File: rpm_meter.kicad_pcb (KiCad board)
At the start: 2 copper layers, 191 parts, among them J1 Conn_01x05_Pin, Q1 BC846, Q10 BC857, Q11 BC857, Q12 BC846, Q13 AO3423, Q14 BC846, Q15 BC846, Q16 BC846, Q17 2N7002H, Q18 2N7002H, Q19 2N7002H, Q2 BC857, Q20 2N7002H, Q21 2N7002H, Q22 2N7002H, Q23 2N7002H, Q24 2N7002H, Q25 2N7002H, Q26 2N7002H, Q27 2N7002H, Q28 2N7002H, Q29 2N7002H, Q3 BC857, Q30 2N7002H, Q31 2N7002H, Q32 2N7002H, Q33 2N7002H, Q34 2N7002H, Q35 2N7002H, Q36 2N7002H, Q37 BC857, Q38 BC857, Q39 BC857, Q4 BC857, Q40 BC857, Q41 BC857, Q42 BC857, Q43 BC857, Q44 BC857, Q45 BC857, Q46 BC857, Q5 BC857, Q6 BC857, Q7 BC857, Q8 BC857, Q9 BC857, U1 M24C02-RMN, U2 STM32C031C6Tx, U3 74LVC1G123, Y1 8

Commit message: Shifting registers
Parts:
- removed D23, D26, D29, D32: LED_Dual_AAKK, Library_local:LED_RG_1210
- removed Q11, Q3, Q38, Q40, Q42, Q44, Q46, Q5, Q7, Q9: BC857, Package_TO_SOT_SMD:SOT-23
- removed Q18, Q20, Q22, Q24, Q26, Q28, Q30, Q32, Q34, Q36: 2N7002H, Package_TO_SOT_SMD:SOT-23
- removed R14, R26, R38: 100, Resistor_SMD:R_0603_1608Metric
- removed R15, R27, R39, R81, R82, R87, R88, R93, R94: 10k, Resistor_SMD:R_0603_1608Metric
- removed R20, R32, R44: 91, Resistor_SMD:R_0603_1608Metric
- removed R21, R33, R45, R9: 22, Resistor_SMD:R_0603_1608Metric
- added C17: 100n, Capacitor_SMD:C_0603_1608Metric, F.Cu at (125.4, 46.3)
- added C18: 100n, Capacitor_SMD:C_0603_1608Metric, F.Cu at (125.4, 48.8)
- added C19: 100n, Capacitor_SMD:C_0603_1608Metric, F.Cu at (125.4, 51.3)
- added C20: 100n, Capacitor_SMD:C_0603_1608Metric, F.Cu at (125.4, 53.8)
- added C21: 100n, Capacitor_SMD:C_0603_1608Metric, F.Cu at (125.4, 56.3)
- added D10: LED_Dual_AAKK, Library_local:LED_RG_1210, F.Cu at (166.9, 108.1)
- added D12: LED_Dual_AAKK, Library_local:LED_RG_1210, F.Cu at (118.0, 83.1)
- added D13: LED_Dual_AAKK, Library_local:LED_RG_1210, F.Cu at (177.8, 108.1)
- added D15: LED_Dual_AAKK, Library_local:LED_RG_1210, F.Cu at (143.8, 113.4)
- added D16: LED_Dual_AAKK, Library_local:LED_RG_1210, F.Cu at (156.0, 75.3)
- added D18: LED_Dual_AAKK, Library_local:LED_RG_1210, F.Cu at (166.9, 75.3)
- added D19: LED_Dual_AAKK, Library_local:LED_RG_1210, F.Cu at (188.7, 91.7)
- added D21: LED_Dual_AAKK, Library_local:LED_RG_1210, F.Cu at (188.7, 108.1)
- added D22: LED_Dual_AAKK, Library_local:LED_RG_1210, F.Cu at (187.4, 47.2)
- added D3: LED_Dual_AAKK, Library_local:LED_RG_1210, F.Cu at (177.8, 75.3)
- added D4: LED_Dual_AAKK, Library_local:LED_RG_1210, F.Cu at (156.0, 91.7)
- added D6: LED_Dual_AAKK, Library_local:LED_RG_1210, F.Cu at (143.8, 97.0)
- added D7: LED_Dual_AAKK, Library_local:LED_RG_1210, F.Cu at (188.7, 75.3)
- added D9: LED_Dual_AAKK, Library_local:LED_RG_1210, F.Cu at (156.0, 108.1)
- added IC1: STPIC6D595TTR, Library_local:SOP65P640X120-16N, F.Cu at (118.9, 48.5)
- added IC2: STPIC6D595TTR, Library_local:SOP65P640X120-16N, F.Cu at (118.9, 55.2)
- added IC3: STPIC6D595TTR, Library_local:SOP65P640X120-16N, F.Cu at (118.9, 62.0)
- added IC4: STPIC6D595TTR, Library_local:SOP65P640X120-16N, F.Cu at (118.9, 68.8)
- added IC5: STPIC6D595TTR, Library_local:SOP65P640X120-16N, F.Cu at (118.9, 75.6)
- added Q47: BC857, Package_TO_SOT_SMD:SOT-23, F.Cu at (176.8, 112.7)
- added Q49: BC857, Package_TO_SOT_SMD:SOT-23, F.Cu at (176.8, 117.3)
- added Q51: BC857, Package_TO_SOT_SMD:SOT-23, F.Cu at (176.8, 96.3)
- added Q53: BC857, Package_TO_SOT_SMD:SOT-23, F.Cu at (176.8, 100.9)
- added Q55: BC857, Package_TO_SOT_SMD:SOT-23, F.Cu at (142.7, 118.0)
- added Q57: BC857, Package_TO_SOT_SMD:SOT-23, F.Cu at (142.7, 122.6)
- added Q59: BC857, Package_TO_SOT_SMD:SOT-23, F.Cu at (155.0, 79.9)
- added Q61: BC857, Package_TO_SOT_SMD:SOT-23, F.Cu at (155.0, 84.5)
- added Q63: BC857, Package_TO_SOT_SMD:SOT-23, F.Cu at (131.8, 101.6)
- added Q65: BC857, Package_TO_SOT_SMD:SOT-23, F.Cu at (131.8, 106.2)
- added Q67: BC857, Package_TO_SOT_SMD:SOT-23, F.Cu at (165.9, 79.9)
- added Q69: BC857, Package_TO_SOT_SMD:SOT-23, F.Cu at (165.9, 84.5)
- added Q71: BC857, Package_TO_SOT_SMD:SOT-23, F.Cu at (187.7, 96.3)
- added Q73: BC857, Package_TO_SOT_SMD:SOT-23, F.Cu at (187.7, 100.9)
- added Q75: BC857, Package_TO_SOT_SMD:SOT-23, F.Cu at (116.9, 104.0)
- added Q77: BC857, Package_TO_SOT_SMD:SOT-23, F.Cu at (116.9, 108.7)
- added Q79: BC857, Package_TO_SOT_SMD:SOT-23, F.Cu at (187.7, 112.7)
- added Q81: BC857, Package_TO_SOT_SMD:SOT-23, F.Cu at (187.7, 117.3)
- added Q83: BC857, Package_TO_SOT_SMD:SOT-23, F.Cu at (186.3, 51.8)
- added Q85: BC857, Package_TO_SOT_SMD:SOT-23, F.Cu at (186.3, 56.4)
- added R101: 91, Resistor_SMD:R_0603_1608Metric, F.Cu at (181.2, 114.1)
- added R102: 22, Resistor_SMD:R_0603_1608Metric, F.Cu at (181.2, 116.6)
- added R103: 100, Resistor_SMD:R_0603_1608Metric, F.Cu at (181.2, 119.1)
- added R104: 10k, Resistor_SMD:R_0603_1608Metric, F.Cu at (181.2, 95.2)
- added R107: 91, Resistor_SMD:R_0603_1608Metric, F.Cu at (181.2, 97.7)
- added R108: 22, Resistor_SMD:R_0603_1608Metric, F.Cu at (181.2, 100.2)
- added R109: 100, Resistor_SMD:R_0603_1608Metric, F.Cu at (181.2, 102.7)
- added R110: 10k, Resistor_SMD:R_0603_1608Metric, F.Cu at (147.2, 116.8)
- added R113: 91, Resistor_SMD:R_0603_1608Metric, F.Cu at (147.2, 119.3)
- added R114: 22, Resistor_SMD:R_0603_1608Metric, F.Cu at (147.2, 121.8)
- added R115: 100, Resistor_SMD:R_0603_1608Metric, F.Cu at (147.2, 124.4)
- added R116: 10k, Resistor_SMD:R_0603_1608Metric, F.Cu at (159.4, 78.8)
- added R119: 91, Resistor_SMD:R_0603_1608Metric, F.Cu at (159.4, 81.3)
- added R120: 22, Resistor_SMD:R_0603_1608Metric, F.Cu at (159.4, 83.8)
- added R121: 100, Resistor_SMD:R_0603_1608Metric, F.Cu at (159.4, 86.3)
- added R122: 10k, Resistor_SMD:R_0603_1608Metric, F.Cu at (136.3, 100.4)
- added R125: 91, Resistor_SMD:R_0603_1608Metric, F.Cu at (136.3, 103.0)
- added R126: 22, Resistor_SMD:R_0603_1608Metric, F.Cu at (136.3, 105.5)
- added R127: 100, Resistor_SMD:R_0603_1608Metric, F.Cu at (136.3, 108.0)
- added R128: 10k, Resistor_SMD:R_0603_1608Metric, F.Cu at (170.3, 78.8)
- added R131: 91, Resistor_SMD:R_0603_1608Metric, F.Cu at (170.3, 81.3)
- added R132: 22, Resistor_SMD:R_0603_1608Metric, F.Cu at (170.3, 83.8)
- added R133: 100, Resistor_SMD:R_0603_1608Metric, F.Cu at (170.3, 86.3)
- added R134: 10k, Resistor_SMD:R_0603_1608Metric, F.Cu at (192.1, 95.2)
- added R137: 91, Resistor_SMD:R_0603_1608Metric, F.Cu at (192.1, 97.7)
- added R138: 22, Resistor_SMD:R_0603_1608Metric, F.Cu at (192.1, 100.2)
- added R139: 100, Resistor_SMD:R_0603_1608Metric, F.Cu at (192.1, 102.7)
- added R140: 10k, Resistor_SMD:R_0603_1608Metric, F.Cu at (121.4, 102.9)
- added R143: 91, Resistor_SMD:R_0603_1608Metric, F.Cu at (121.4, 105.4)
- added R144: 22, Resistor_SMD:R_0603_1608Metric, F.Cu at (121.4, 107.9)
- added R145: 100, Resistor_SMD:R_0603_1608Metric, F.Cu at (121.4, 110.4)
- added R146: 10k, Resistor_SMD:R_0603_1608Metric, F.Cu at (192.1, 111.6)
- added R149: 91, Resistor_SMD:R_0603_1608Metric, F.Cu at (192.1, 114.1)
- added R150: 22, Resistor_SMD:R_0603_1608Metric, F.Cu at (192.1, 116.6)
- added R151: 100, Resistor_SMD:R_0603_1608Metric, F.Cu at (192.1, 119.1)
- added R152: 10k, Resistor_SMD:R_0603_1608Metric, F.Cu at (190.8, 50.6)
- added R155: 91, Resistor_SMD:R_0603_1608Metric, F.Cu at (190.8, 53.1)
- added R156: 22, Resistor_SMD:R_0603_1608Metric, F.Cu at (190.8, 55.6)
- added R157: 100, Resistor_SMD:R_0603_1608Metric, F.Cu at (190.8, 58.2)
- added R98: 10k, Resistor_SMD:R_0603_1608Metric, F.Cu at (181.2, 111.6)
- Q17, Q19, Q21, Q23, Q25, Q27, Q29, Q31, Q33, Q35: value 2N7002H -> BC857
- R10, R22, R34, R46: value 100 -> 91
- R11, R23, R35, R78, R84, R90, R96: value 10k -> 22
- R12, R24, R36: value 91 -> 100
- R13, R25, R37: value 22 -> 10k
- R79, R85, R91, R97: value 10k -> 100
- R8: value 91 -> 10k
- R83, R89, R95: value 10k -> 91
- moved R8 89.5 mm to (125.4, 58.8)
- moved C2 86.6 mm to (175.0, 48.8)
- moved D2 86.6 mm to (179.3, 58.9)
- moved R3 86.6 mm to (175.0, 56.3)
- moved R6 86.6 mm to (175.0, 63.9)
- moved TP1 86.6 mm to (179.3, 47.4)
- moved C1 86.6 mm to (175.0, 46.3)
- moved D1 86.6 mm to (179.3, 55.8)
- moved Q1 86.6 mm to (179.5, 62.8)
- moved R1 86.6 mm to (175.0, 51.3)
- moved R2 86.6 mm to (175.0, 53.8)
- moved R4 86.6 mm to (175.0, 58.8)
- moved TP2 86.6 mm to (179.3, 52.0)
- moved R5 86.6 mm to (175.0, 61.3)
- moved D5 70.4 mm to (118.0, 115.8)
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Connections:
- net /led_segment3/led_net_2_1 renamed /Leds/led_segment11/led_net_2_1
- net /led_segment5/led_net_2_1 renamed /Leds/led_segment17/led_net_2_1
- D11 pad 1: /led_segment2/led_net_2_1 -> /Leds/led_segment8/led_net_2_1
- D11 pad 2: /led_segment2/led_net_2_1 -> /Leds/led_segment8/led_net_2_1
- D11 pad 3: /led_segment2/led_net_2_2 -> /Leds/led_segment8/led_net_2_2
- D11 pad 4: /led_segment2/led_net_2_4 -> /Leds/led_segment8/led_net_2_4
- D14 pad 3: /led_segment3/led_net_2_2 -> /Leds/led_segment11/led_net_2_2
- D14 pad 4: /led_segment3/led_net_2_4 -> /Leds/led_segment11/led_net_2_4
- D17 pad 1: /led_segment4/led_net_2_1 -> /Leds/led_segment14/led_net_2_1
- D17 pad 2: /led_segment4/led_net_2_1 -> /Leds/led_segment14/led_net_2_1
- D17 pad 3: /led_segment4/led_net_2_2 -> /Leds/led_segment14/led_net_2_2
- D17 pad 4: /led_segment4/led_net_2_4 -> /Leds/led_segment14/led_net_2_4
- D20 pad 3: /led_segment5/led_net_2_2 -> /Leds/led_segment17/led_net_2_2
- D20 pad 4: /led_segment5/led_net_2_4 -> /Leds/led_segment17/led_net_2_4
- D5 pad 1: /led_segment0/led_net_2_1 -> /Leds/led_segment2/led_net_2_1
- D5 pad 2: /led_segment0/led_net_2_1 -> /Leds/led_segment2/led_net_2_1
- D5 pad 3: /led_segment0/led_net_2_2 -> /Leds/led_segment2/led_net_2_2
- D5 pad 4: /led_segment0/led_net_2_4 -> /Leds/led_segment2/led_net_2_4
- D8 pad 1: /led_segment1/led_net_2_1 -> /Leds/led_segment5/led_net_2_1
- D8 pad 2: /led_segment1/led_net_2_1 -> /Leds/led_segment5/led_net_2_1
- D8 pad 3: /led_segment1/led_net_2_2 -> /Leds/led_segment5/led_net_2_2
- D8 pad 4: /led_segment1/led_net_2_4 -> /Leds/led_segment5/led_net_2_4
- Q10 pad 1: Net-(Q10-B) -> /Leds/led_segment2/led_net_1_1
- Q10 pad 2: /led_segment8/led_net_1_1 -> +5V_led
- Q10 pad 3: /led_segment8/led_net_2_1 -> Net-(Q10-C)
- Q17 pad 1: Net-(Q17-G) -> Net-(Q10-C)
- Q17 pad 2: GND -> /Leds/led_segment2/led_net_1_1
- Q17 pad 3: /led_segment0/led_net_2_5 -> /Leds/led_segment2/led_net_2_1
- Q19 pad 1: Net-(Q19-G) -> /Leds/led_segment3/led_net_1_1
- Q19 pad 2: GND -> +5V_led
- Q19 pad 3: /led_segment2/led_net_2_5 -> Net-(Q19-C)
- Q2 pad 1: Net-(Q2-B) -> /Leds/led_segment0/led_net_1_1
- Q2 pad 2: /led_segment0/led_net_1_1 -> +5V_led
- Q2 pad 3: /led_segment0/led_net_2_1 -> Net-(Q2-C)
- Q21 pad 1: Net-(Q21-G) -> Net-(Q19-C)
- Q21 pad 2: GND -> /Leds/led_segment3/led_net_1_1
- Q21 pad 3: /led_segment4/led_net_2_5 -> /Leds/led_segment3/led_net_2_1
- Q23 pad 1: Net-(Q23-G) -> /Leds/led_segment4/led_net_1_1
- Q23 pad 2: GND -> +5V_led
- Q23 pad 3: /led_segment6/led_net_2_5 -> Net-(Q23-C)
- Q25 pad 1: Net-(Q25-G) -> Net-(Q23-C)
- Q25 pad 2: GND -> /Leds/led_segment4/led_net_1_1
- Q25 pad 3: /led_segment8/led_net_2_5 -> /Leds/led_segment4/led_net_2_1
- Q27 pad 1: Net-(Q27-G) -> /Leds/led_segment5/led_net_1_1
- Q27 pad 2: GND -> +5V_led
- Q27 pad 3: /led_segment0/led_net_2_3 -> Net-(Q27-C)
- Q29 pad 1: Net-(Q29-G) -> Net-(Q27-C)
- Q29 pad 2: GND -> /Leds/led_segment5/led_net_1_1
- Q29 pad 3: /led_segment2/led_net_2_3 -> /Leds/led_segment5/led_net_2_1
- Q31 pad 1: Net-(Q31-G) -> /Leds/led_segment6/led_net_1_1
- Q31 pad 2: GND -> +5V_led
- Q31 pad 3: /led_segment4/led_net_2_3 -> Net-(Q31-C)
- Q33 pad 1: Net-(Q33-G) -> Net-(Q31-C)
- Q33 pad 2: GND -> /Leds/led_segment6/led_net_1_1
- Q33 pad 3: /led_segment6/led_net_2_3 -> /Leds/led_segment6/led_net_2_1
- Q35 pad 1: Net-(Q35-G) -> /Leds/led_segment7/led_net_1_1
- Q35 pad 2: GND -> +5V_led
- Q35 pad 3: /led_segment8/led_net_2_3 -> Net-(Q35-C)
- Q37 pad 1: /led_segment0/led_net_1_1 -> Net-(Q35-C)
- Q37 pad 2: +5V_led -> /Leds/led_segment7/led_net_1_1
- Q37 pad 3: Net-(Q2-B) -> /Leds/led_segment7/led_net_2_1
- Q39 pad 1: /led_segment2/led_net_1_1 -> /Leds/led_segment8/led_net_1_1
- Q4 pad 1: Net-(Q39-C) -> Net-(Q2-C)
- Q4 pad 2: /led_segment2/led_net_1_1 -> /Leds/led_segment0/led_net_1_1
- Q4 pad 3: /led_segment2/led_net_2_1 -> /Leds/led_segment0/led_net_2_1
- Q41 pad 1: /led_segment4/led_net_1_1 -> Net-(Q39-C)
- Q41 pad 2: +5V_led -> /Leds/led_segment8/led_net_1_1
- Q41 pad 3: Net-(Q41-C) -> /Leds/led_segment8/led_net_2_1
- Q43 pad 1: /led_segment6/led_net_1_1 -> /Leds/led_segment9/led_net_1_1
- Q45 pad 1: /led_segment8/led_net_1_1 -> Net-(Q43-C)
- Q45 pad 2: +5V_led -> /Leds/led_segment9/led_net_1_1
- Q45 pad 3: Net-(Q10-B) -> /Leds/led_segment9/led_net_2_1
- Q6 pad 1: Net-(Q41-C) -> /Leds/led_segment1/led_net_1_1
- Q6 pad 2: /led_segment4/led_net_1_1 -> +5V_led
- Q6 pad 3: /led_segment4/led_net_2_1 -> Net-(Q6-C)
- Q8 pad 1: Net-(Q43-C) -> Net-(Q6-C)
- Q8 pad 2: /led_segment6/led_net_1_1 -> /Leds/led_segment1/led_net_1_1
- Q8 pad 3: /led_segment6/led_net_2_1 -> /Leds/led_segment1/led_net_2_1
- R10 pad 1: /led_segment0/led_net_2_2 -> /Leds/led_segment0/led_net_2_4
- R10 pad 2: /led_segment0/led_net_2_3 -> /Leds/red0
- R11 pad 1: Net-(Q3-B) -> +5V_led
- R11 pad 2: GND -> /Leds/led_segment0/led_net_1_1
- R12 pad 1: /led_segment1/led_net_2_4 -> /Leds/led_segment0/led_net_2_2
- R12 pad 2: /led_segment1/led_net_2_5 -> /Leds/green0
- R13 pad 1: +5V_led -> Net-(Q6-C)
- R13 pad 2: /led_segment1/led_net_1_1 -> GND
- R16 pad 1: /led_segment2/led_net_2_4 -> /Leds/led_segment1/led_net_2_4
- R16 pad 2: /led_segment2/led_net_2_5 -> /Leds/red1
- R17 pad 2: /led_segment2/led_net_1_1 -> /Leds/led_segment1/led_net_1_1
- R18 pad 1: /led_segment2/led_net_2_2 -> /Leds/led_segment1/led_net_2_2
- R18 pad 2: /led_segment2/led_net_2_3 -> /Leds/green1
- R19 pad 1: Net-(Q40-C) -> Net-(Q10-C)
- R22 pad 1: /led_segment3/led_net_2_2 -> /Leds/led_segment2/led_net_2_4
- R22 pad 2: /led_segment3/led_net_2_3 -> /Leds/red2
- R23 pad 1: Net-(Q41-C) -> +5V_led
- R23 pad 2: GND -> /Leds/led_segment2/led_net_1_1
- R24 pad 1: /led_segment4/led_net_2_4 -> /Leds/led_segment2/led_net_2_2
- R24 pad 2: /led_segment4/led_net_2_5 -> /Leds/green2
- R25 pad 1: +5V_led -> Net-(Q19-C)
- R25 pad 2: /led_segment4/led_net_1_1 -> GND
- R28 pad 1: /led_segment5/led_net_2_4 -> /Leds/led_segment3/led_net_2_4
- R28 pad 2: /led_segment5/led_net_2_5 -> /Leds/red3
- R29 pad 2: /led_segment5/led_net_1_1 -> /Leds/led_segment3/led_net_1_1
- R30 pad 1: /led_segment5/led_net_2_2 -> /Leds/led_segment3/led_net_2_2
- R30 pad 2: /led_segment5/led_net_2_3 -> /Leds/green3
- R31 pad 1: Net-(Q43-C) -> Net-(Q23-C)
- R34 pad 1: /led_segment6/led_net_2_2 -> /Leds/led_segment4/led_net_2_4
- R34 pad 2: /led_segment6/led_net_2_3 -> /Leds/red4
- R35 pad 1: Net-(Q44-C) -> +5V_led
- R35 pad 2: GND -> /Leds/led_segment4/led_net_1_1
- R36 pad 1: /led_segment7/led_net_2_4 -> /Leds/led_segment4/led_net_2_2
- R36 pad 2: /led_segment7/led_net_2_5 -> /Leds/green4
- R37 pad 1: +5V_led -> Net-(Q27-C)
- R37 pad 2: /led_segment7/led_net_1_1 -> GND
- R40 pad 1: /led_segment8/led_net_2_4 -> /Leds/led_segment5/led_net_2_4
- R40 pad 2: /led_segment8/led_net_2_5 -> /Leds/red5
- R41 pad 2: /led_segment8/led_net_1_1 -> /Leds/led_segment5/led_net_1_1
- R42 pad 1: /led_segment8/led_net_2_2 -> /Leds/led_segment5/led_net_2_2
- R42 pad 2: /led_segment8/led_net_2_3 -> /Leds/green5
- R43 pad 1: Net-(Q11-B) -> Net-(Q31-C)
- R46 pad 1: /led_segment9/led_net_2_2 -> /Leds/led_segment6/led_net_2_4
- R46 pad 2: /led_segment9/led_net_2_3 -> /Leds/red6
- R7 pad 1: Net-(Q2-B) -> Net-(Q2-C)
- R78 pad 1: /red0 -> +5V_led
- R78 pad 2: Net-(Q17-G) -> /Leds/led_segment6/led_net_1_1
- R79 pad 1: /red1 -> /Leds/led_segment6/led_net_2_2
- R79 pad 2: Net-(Q18-G) -> /Leds/green6
- R8 pad 1: /led_segment0/led_net_2_4 -> Net-(IC5-SER_OUT)
- R8 pad 2: /led_segment0/led_net_2_5 -> GND
- R80 pad 1: /red2 -> Net-(Q35-C)
- R80 pad 2: Net-(Q19-G) -> GND
- R83 pad 1: /red5 -> /Leds/led_segment7/led_net_2_4
- R83 pad 2: Net-(Q22-G) -> /Leds/red7
- R84 pad 1: /red6 -> +5V_led
- R84 pad 2: Net-(Q23-G) -> /Leds/led_segment7/led_net_1_1
- R85 pad 1: /red7 -> /Leds/led_segment7/led_net_2_2
- R85 pad 2: Net-(Q24-G) -> /Leds/green7
- R86 pad 1: /red8 -> Net-(Q39-C)
- R86 pad 2: Net-(Q25-G) -> GND
- R89 pad 1: /green1 -> /Leds/led_segment8/led_net_2_4
- R89 pad 2: Net-(Q28-G) -> /Leds/red8
- R90 pad 1: /green2 -> +5V_led
- R90 pad 2: Net-(Q29-G) -> /Leds/led_segment8/led_net_1_1
- R91 pad 1: /green3 -> /Leds/led_segment8/led_net_2_2
- R91 pad 2: Net-(Q30-G) -> /Leds/green8
- R92 pad 1: /green4 -> Net-(Q43-C)
- R92 pad 2: Net-(Q31-G) -> GND
- R95 pad 1: /green7 -> /Leds/led_segment9/led_net_2_4
- R95 pad 2: Net-(Q34-G) -> /Leds/red9
- R96 pad 1: /green8 -> +5V_led
- R96 pad 2: Net-(Q35-G) -> /Leds/led_segment9/led_net_1_1
- R97 pad 1: /green9 -> /Leds/led_segment9/led_net_2_2
- R97 pad 2: Net-(Q36-G) -> /Leds/green9
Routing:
- net /mcu/NRST: track 16.0 -> 0.00 mm, vias 1 -> 0
- net /mcu/TMS: track 8.06 -> 0.00 mm
- net +3.3V: track 5.42 -> 0.00 mm
- net GND: track 4.69 -> 0.00 mm
- net /mcu/TCK: track 4.50 -> 0.00 mm

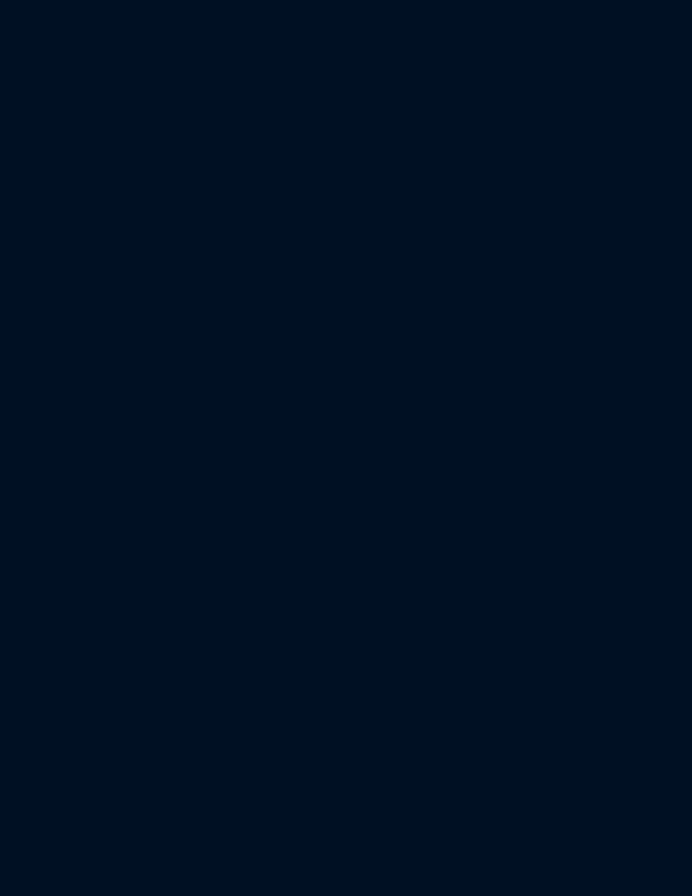
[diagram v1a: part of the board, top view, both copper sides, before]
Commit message: Step_down 5v
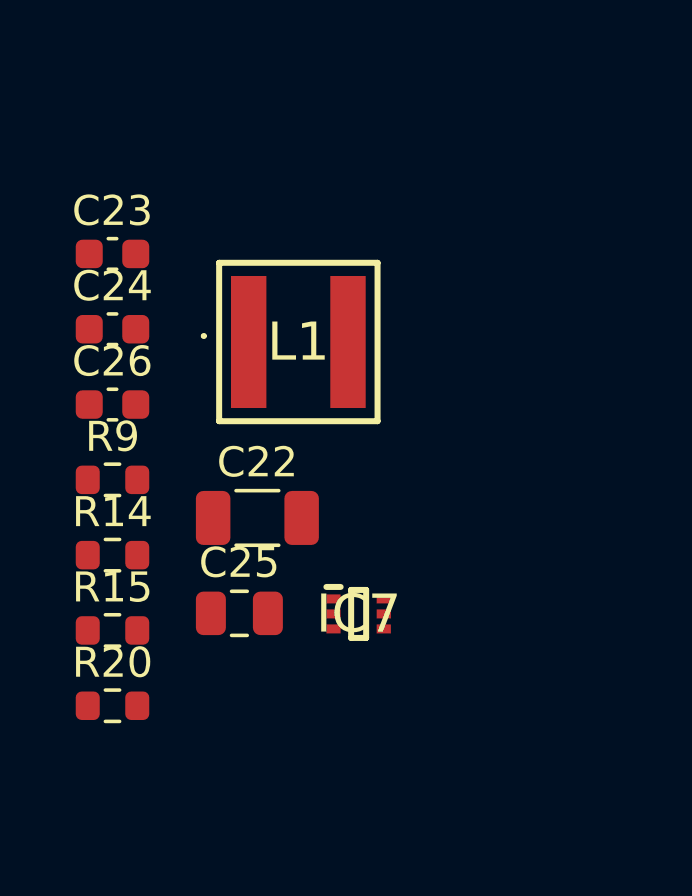
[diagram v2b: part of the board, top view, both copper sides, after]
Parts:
- added C22: 10uF, Capacitor_SMD:C_1206_3216Metric, F.Cu at (98.1, 116.8)
- added C23: 100nF, Capacitor_SMD:C_0603_1608Metric, F.Cu at (93.3, 108.0)
- added C24: 33pF, Capacitor_SMD:C_0603_1608Metric, F.Cu at (93.3, 110.5)
- added C25: 22uF, Capacitor_SMD:C_0805_2012Metric, F.Cu at (97.5, 120.0)
- added C26: 100nF, Capacitor_SMD:C_0603_1608Metric, F.Cu at (93.3, 113.0)
- added IC7: TPS566247DRLR, Library_local:SOTFL50P160X60-6N, F.Cu at (101.5, 120.0)
- added L1: 2.2uH, Library_local:XAL5030222MEC, F.Cu at (99.5, 110.9)
- added R14: 12k4, Resistor_SMD:R_0603_1608Metric, F.Cu at (93.3, 118.0)
- added R15: 220k, Resistor_SMD:R_0603_1608Metric, F.Cu at (93.3, 120.5)
- added R20: 30k, Resistor_SMD:R_0603_1608Metric, F.Cu at (93.3, 123.0)
- added R9: 100k, Resistor_SMD:R_0603_1608Metric, F.Cu at (93.3, 115.5)

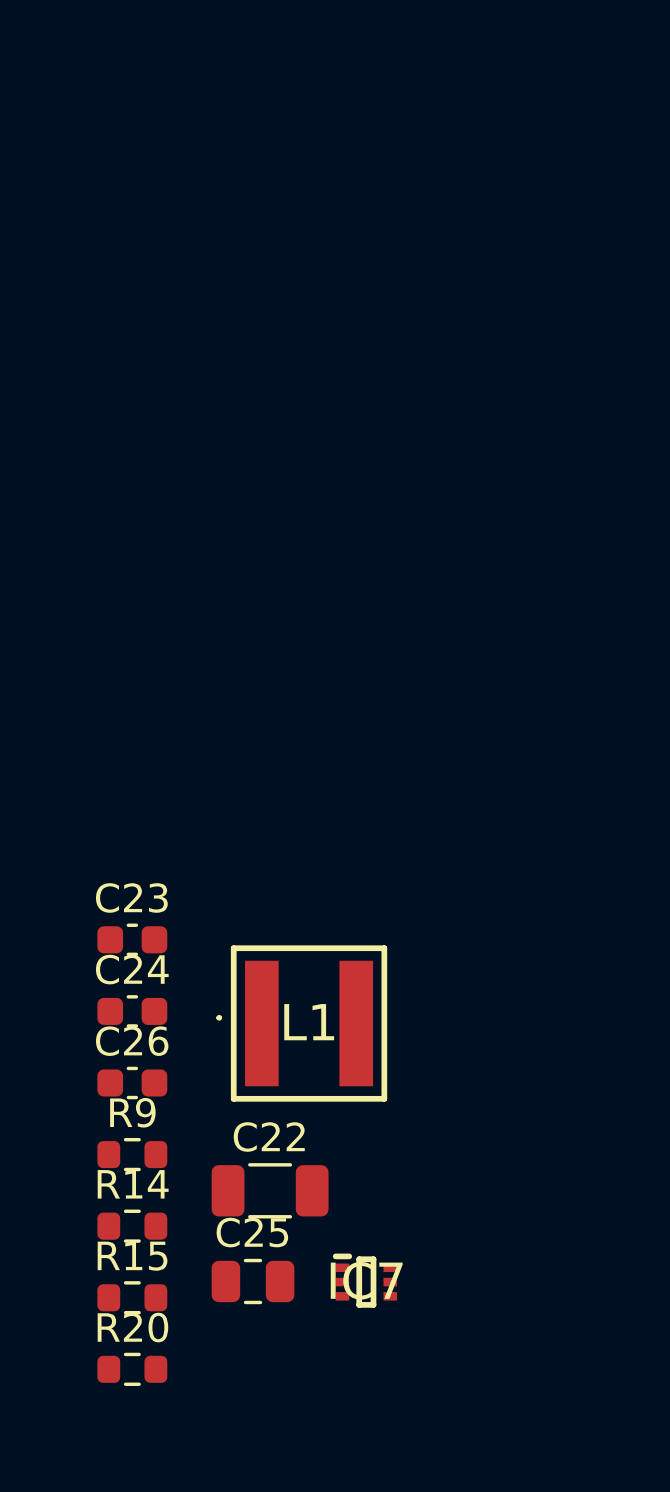
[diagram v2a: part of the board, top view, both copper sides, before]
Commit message: LDO 3v3
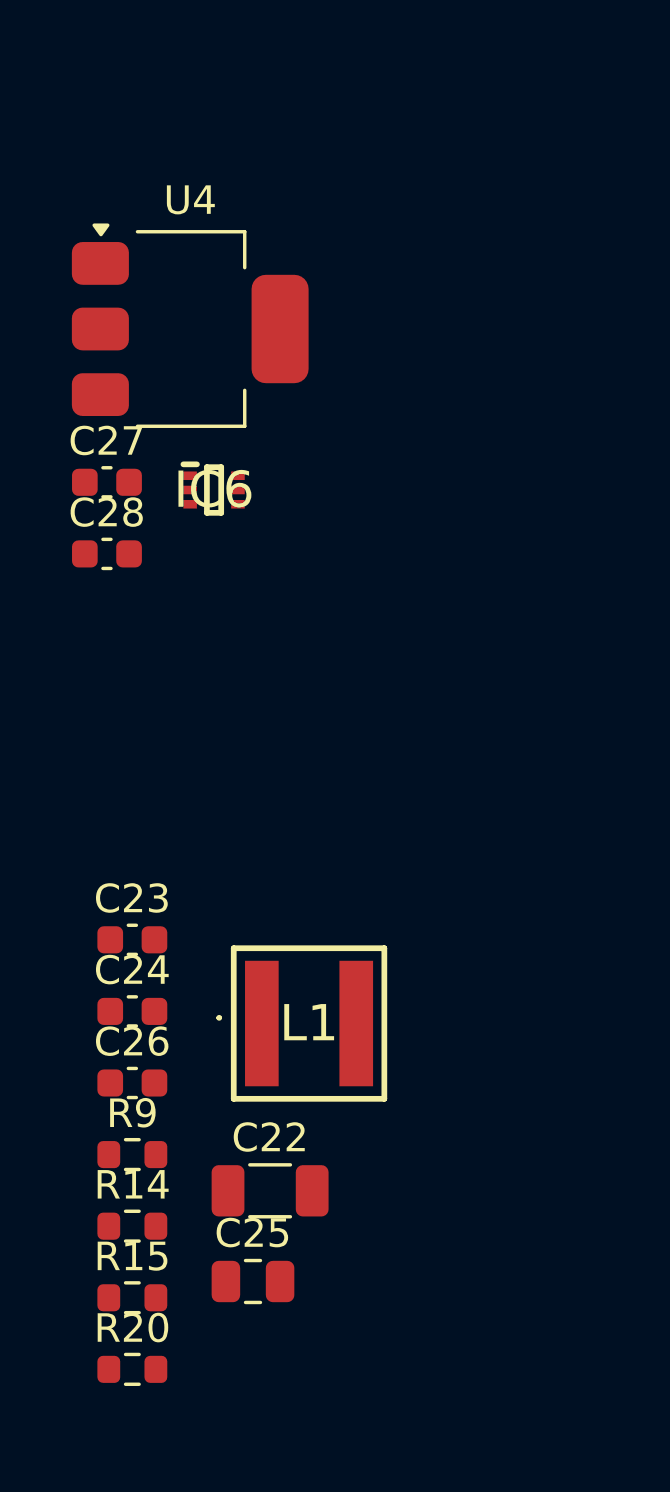
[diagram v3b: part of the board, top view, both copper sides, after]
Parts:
- removed IC7: TPS566247DRLR, Library_local:SOTFL50P160X60-6N
- added C27: 1u, Capacitor_SMD:C_0603_1608Metric, F.Cu at (92.4, 92.0)
- added C28: 1u, Capacitor_SMD:C_0603_1608Metric, F.Cu at (92.4, 94.5)
- added IC6: TPS566247DRLR, Library_local:SOTFL50P160X60-6N, F.Cu at (96.1, 92.2)
- added U4: TLV1117-33, Package_TO_SOT_SMD:SOT-223-3_TabPin2, F.Cu at (95.3, 86.6)

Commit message: ignore
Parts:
- moved C22 9.90 mm to (108.0, 117.6)
- moved C23 9.90 mm to (103.1, 108.8)
- moved C24 9.90 mm to (103.1, 111.3)
- moved C26 9.90 mm to (103.1, 113.8)
- moved C27 9.90 mm to (102.2, 92.8)
- moved C28 9.90 mm to (102.2, 95.3)
- moved R14 9.90 mm to (103.1, 118.8)
- moved R15 9.90 mm to (103.1, 121.3)
- moved R20 9.90 mm to (103.1, 123.8)
- moved R9 9.90 mm to (103.1, 116.3)
- moved U4 9.90 mm to (105.2, 87.4)
- moved C25 9.90 mm to (107.4, 120.8)
- moved IC6 9.90 mm to (106.0, 93.0)
- moved L1 9.90 mm to (109.3, 111.7)
- moved R146 4.12 mm to (196.2, 111.2)
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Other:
- board outline added: 122.3 x 96.7 mm
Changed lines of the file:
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@@
 	(footprint "Resistor_SMD:R_0603_1608Metric"
 		(layer "F.Cu")
-		(at 93.267 118.03)
+		(at 103.135 118.83)
 		(descr "Resistor SMD 0603 (1608 Metric), square (rectangular) end terminal, IPC_7351 nominal, (Body size source: IPC-SM-782 page 72, https://www.pcb-3d.com/wordpress/wp-content/uploads/ipc-sm-782a_amendment_1_and_2.pdf), generated with kicad-footprint-generator")
 		(tags "resistor")
@@
 	(footprint "Library_local:LED_RG_1210"
 		(layer "F.Cu")
-		(at 188.705 108.13)
+		(at 192.815 107.81)
 		(descr "RGB LED 3.2x2.7mm http://www.avagotech.com/docs/AV02-0610EN")
 		(tags "LED 3227")
@@
 	(footprint "Capacitor_SMD:C_0603_1608Metric"
 		(layer "F.Cu")
-		(at 93.267 113.01)
+		(at 103.135 113.81)
 		(descr "Capacitor SMD 0603 (1608 Metric), square (rectangular) end terminal, IPC_7351 nominal, (Body size source: IPC-SM-782 page 76, https://www.pcb-3d.com/wordpress/wp-content/uploads/ipc-sm-782a_amendment_1_and_2.pdf), generated with kicad-footprint-generator")
 		(tags "capacitor")
@@
 	(footprint "Resistor_SMD:R_0603_1608Metric"
 		(layer "F.Cu")
-		(at 93.267 123.05)
+		(at 103.135 123.85)
 		(descr "Resistor SMD 0603 (1608 Metric), square (rectangular) end terminal, IPC_7351 nominal, (Body size source: IPC-SM-782 page 72, https://www.pcb-3d.com/wordpress/wp-content/uploads/ipc-sm-782a_amendment_1_and_2.pdf), generated with kicad-footprint-generator")
 		(tags "resistor")
@@
 	(footprint "Capacitor_SMD:C_0805_2012Metric"
 		(layer "F.Cu")
-		(at 97.497 119.97)
+		(at 107.365 120.77)
 		(descr "Capacitor SMD 0805 (2012 Metric), square (rectangular) end terminal, IPC_7351 nominal, (Body size source: IPC-SM-782 page 76, https://www.pcb-3d.com/wordpress/wp-content/uploads/ipc-sm-782a_amendment_1_and_2.pdf, https://docs.google.com/spreadsheets/d/1BsfQQcO9C6DZCsRaXUlFlo91Tg2WpOkGARC1WS5S8t0/edit?usp=sharing), generated with kicad-footprint-generator")
 		(tags "capacitor")
@@
 	(footprint "Package_TO_SOT_SMD:SOT-23"
 		(layer "F.Cu")
-		(at 187.675 112.705)
+		(at 191.785 112.385)
 		(descr "SOT, 3 Pin (https://www.jedec.org/system/files/docs/to-236h.pdf variant AB), generated with kicad-footprint-generator ipc_gullwing_generator.py")
 		(tags "SOT TO_SOT_SMD")
@@
 	(footprint "Capacitor_SMD:C_0603_1608Metric"
 		(layer "F.Cu")
-		(at 92.377 94.46)
+		(at 102.245 95.26)
 		(descr "Capacitor SMD 0603 (1608 Metric), square (rectangular) end terminal, IPC_7351 nominal, (Body size source: IPC-SM-782 page 76, https://www.pcb-3d.com/wordpress/wp-content/uploads/ipc-sm-782a_amendment_1_and_2.pdf), generated with kicad-footprint-generator")
 		(tags "capacitor")
@@
 	(footprint "Capacitor_SMD:C_0603_1608Metric"
 		(layer "F.Cu")
-		(at 93.267 107.99)
+		(at 103.135 108.79)
 		(descr "Capacitor SMD 0603 (1608 Metric), square (rectangular) end terminal, IPC_7351 nominal, (Body size source: IPC-SM-782 page 76, https://www.pcb-3d.com/wordpress/wp-content/uploads/ipc-sm-782a_amendment_1_and_2.pdf), generated with kicad-footprint-generator")
 		(tags "capacitor")
@@
 	(footprint "Resistor_SMD:R_0603_1608Metric"
 		(layer "F.Cu")
-		(at 192.125 116.58)
+		(at 196.235 116.26)
 		(descr "Resistor SMD 0603 (1608 Metric), square (rectangular) end terminal, IPC_7351 nominal, (Body size source: IPC-SM-782 page 72, https://www.pcb-3d.com/wordpress/wp-content/uploads/ipc-sm-782a_amendment_1_and_2.pdf), generated with kicad-footprint-generator")
 		(tags "resistor")
@@
 	(footprint "Capacitor_SMD:C_0603_1608Metric"
 		(layer "F.Cu")
-		(at 92.377 91.95)
+		(at 102.245 92.75)
 		(descr "Capacitor SMD 0603 (1608 Metric), square (rectangular) end terminal, IPC_7351 nominal, (Body size source: IPC-SM-782 page 76, https://www.pcb-3d.com/wordpress/wp-content/uploads/ipc-sm-782a_amendment_1_and_2.pdf), generated with kicad-footprint-generator")
 		(tags "capacitor")
@@
 	(footprint "Package_TO_SOT_SMD:SOT-23"
 		(layer "F.Cu")
-		(at 187.675 117.33)
+		(at 191.785 117.01)
 		(descr "SOT, 3 Pin (https://www.jedec.org/system/files/docs/to-236h.pdf variant AB), generated with kicad-footprint-generator ipc_gullwing_generator.py")
 		(tags "SOT TO_SOT_SMD")
@@
 	(footprint "Library_local:XAL5030222MEC"
 		(layer "F.Cu")
-		(at 99.462 110.925)
+		(at 109.33 111.725)
 		(descr "XAL5030-222MEC-3")
 		(tags "Inductor")
@@
 	(footprint "Capacitor_SMD:C_1206_3216Metric"
 		(layer "F.Cu")
-		(at 98.097 116.79)
+		(at 107.965 117.59)
 		(descr "Capacitor SMD 1206 (3216 Metric), square (rectangular) end terminal, IPC_7351 nominal, (Body size source: IPC-SM-782 page 76, https://www.pcb-3d.com/wordpress/wp-content/uploads/ipc-sm-782a_amendment_1_and_2.pdf), generated with kicad-footprint-generator")
 		(tags "capacitor")
@@
 	(footprint "Library_local:SOTFL50P160X60-6N"
 		(layer "F.Cu")
-		(at 96.132 92.22)
+		(at 106 93.02)
 		(descr "DRL0006A")
 		(tags "Integrated Circuit")
@@
 	(footprint "Resistor_SMD:R_0603_1608Metric"
 		(layer "F.Cu")
-		(at 192.125 114.07)
+		(at 196.235 113.75)
 		(descr "Resistor SMD 0603 (1608 Metric), square (rectangular) end terminal, IPC_7351 nominal, (Body size source: IPC-SM-782 page 72, https://www.pcb-3d.com/wordpress/wp-content/uploads/ipc-sm-782a_amendment_1_and_2.pdf), generated with kicad-footprint-generator")
 		(tags "resistor")
@@
 	(footprint "Resistor_SMD:R_0603_1608Metric"
 		(layer "F.Cu")
-		(at 192.125 119.09)
+		(at 196.235 118.77)
 		(descr "Resistor SMD 0603 (1608 Metric), square (rectangular) end terminal, IPC_7351 nominal, (Body size source: IPC-SM-782 page 72, https://www.pcb-3d.com/wordpress/wp-content/uploads/ipc-sm-782a_amendment_1_and_2.pdf), generated with kicad-footprint-generator")
 		(tags "resistor")
@@
 	(footprint "Resistor_SMD:R_0603_1608Metric"
 		(layer "F.Cu")
-		(at 93.267 120.54)
+		(at 103.135 121.34)
 		(descr "Resistor SMD 0603 (1608 Metric), square (rectangular) end terminal, IPC_7351 nominal, (Body size source: IPC-SM-782 page 72, https://www.pcb-3d.com/wordpress/wp-content/uploads/ipc-sm-782a_amendment_1_and_2.pdf), generated with kicad-footprint-generator")
 		(tags "resistor")
@@
 	(footprint "Resistor_SMD:R_0603_1608Metric"
 		(layer "F.Cu")
-		(at 192.125 111.56)
+		(at 196.235 111.24)
 		(descr "Resistor SMD 0603 (1608 Metric), square (rectangular) end terminal, IPC_7351 nominal, (Body size source: IPC-SM-782 page 72, https://www.pcb-3d.com/wordpress/wp-content/uploads/ipc-sm-782a_amendment_1_and_2.pdf), generated with kicad-footprint-generator")
 		(tags "resistor")
@@
 	(footprint "Capacitor_SMD:C_0603_1608Metric"
 		(layer "F.Cu")
-		(at 93.267 110.5)
+		(at 103.135 111.3)
 		(descr "Capacitor SMD 0603 (1608 Metric), square (rectangular) end terminal, IPC_7351 nominal, (Body size source: IPC-SM-782 page 76, https://www.pcb-3d.com/wordpress/wp-content/uploads/ipc-sm-782a_amendment_1_and_2.pdf), generated with kicad-footprint-generator")
 		(tags "capacitor")
@@
 	(footprint "Resistor_SMD:R_0603_1608Metric"
 		(layer "F.Cu")
-		(at 93.267 115.52)
+		(at 103.135 116.32)
 		(descr "Resistor SMD 0603 (1608 Metric), square (rectangular) end terminal, IPC_7351 nominal, (Body size source: IPC-SM-782 page 72, https://www.pcb-3d.com/wordpress/wp-content/uploads/ipc-sm-782a_amendment_1_and_2.pdf), generated with kicad-footprint-generator")
 		(tags "resistor")
@@
 	(footprint "Package_TO_SOT_SMD:SOT-223-3_TabPin2"
 		(layer "F.Cu")
-		(at 95.297 86.575)
+		(at 105.165 87.375)
 		(descr "module CMS SOT223 4 pins")
 		(tags "CMS SOT")
@@
 		)
 	)
+	(gr_rect
+		(start 83.09 36.65)
+		(end 205.37 133.31)
+		(stroke
+			(width 0.05)
+			(type default)
+		)
+		(fill none)
+		(layer "Edge.Cuts")
+	)
 )
